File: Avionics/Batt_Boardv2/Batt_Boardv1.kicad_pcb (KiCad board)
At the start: 2 copper layers, 90.2 x 95.9 mm, 30 parts, among them J1 Conn_02x26_Odd_Even, J2 Conn_02x26_Odd_Even, Q1 IRF7458, Q2 IRF7458, U3 TMP36xS

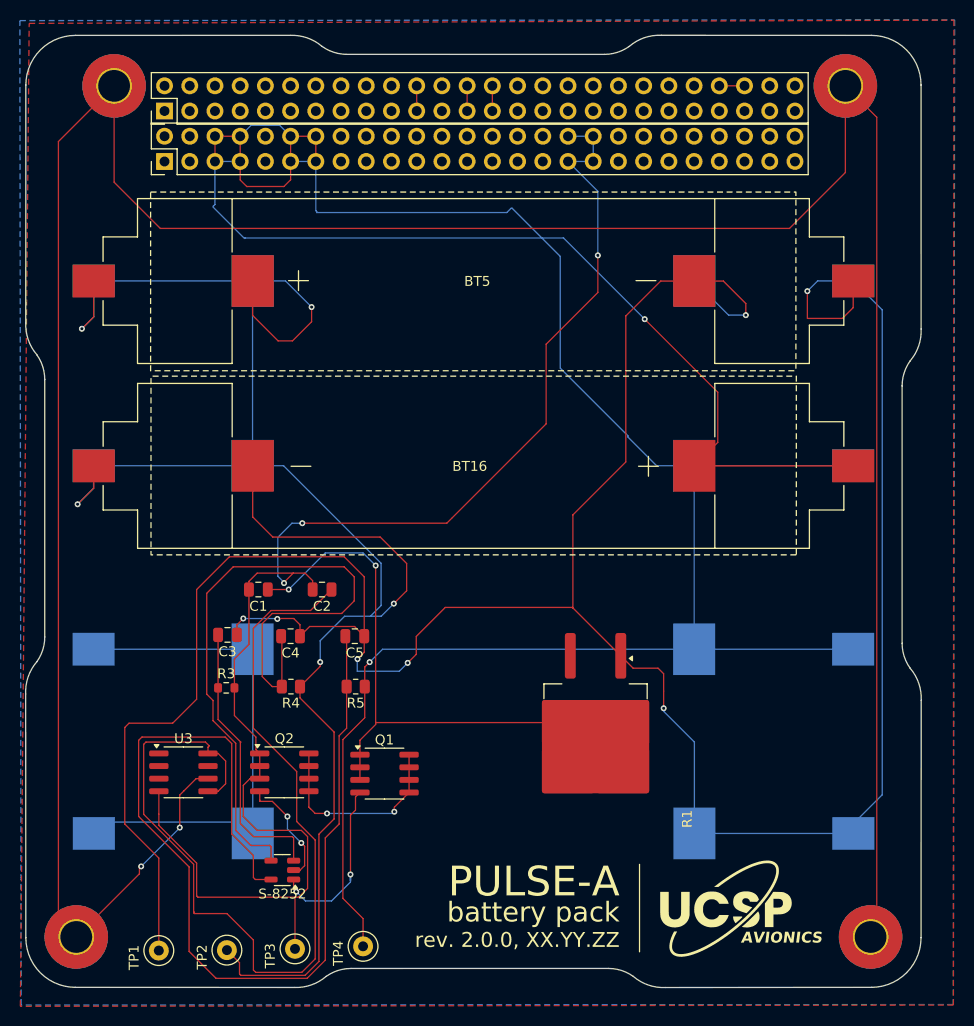
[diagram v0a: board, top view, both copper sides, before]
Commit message: zones added, but incorrectly
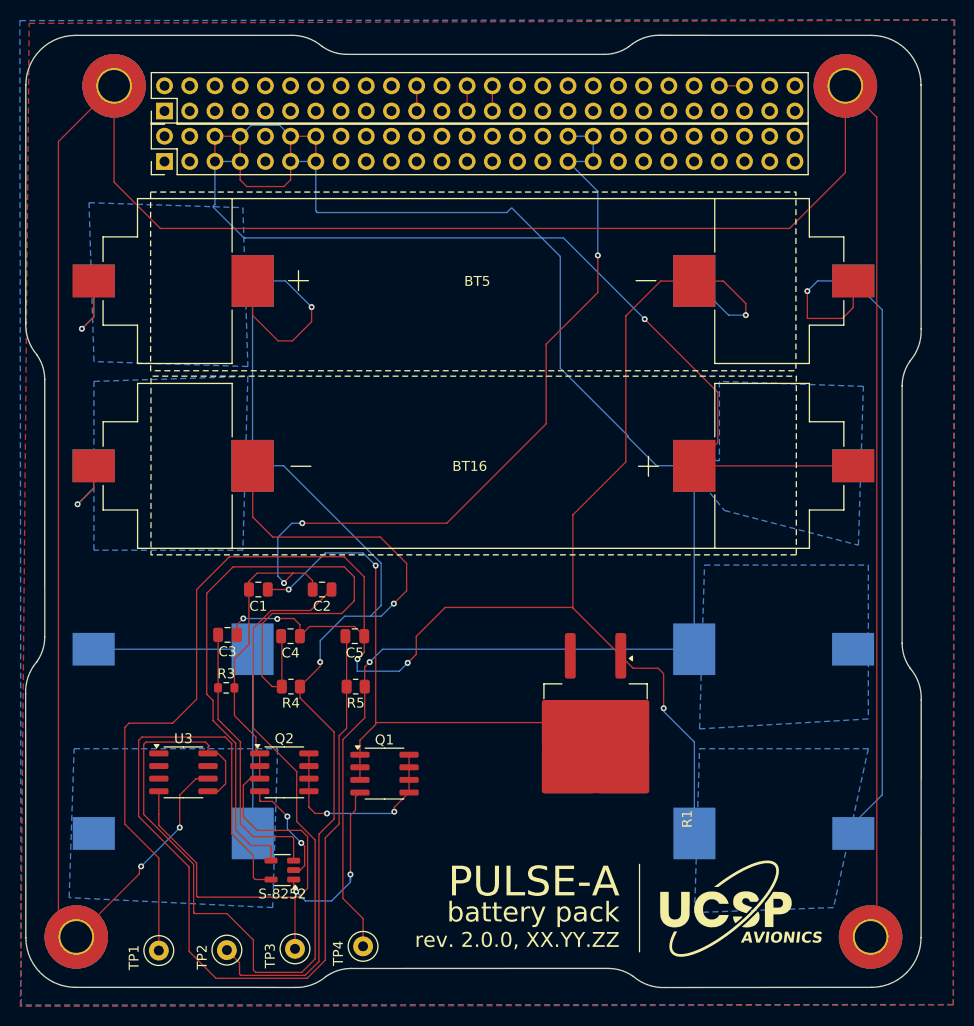
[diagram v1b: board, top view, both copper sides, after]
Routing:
- net /BATT_PRE_INH: track 298.4 -> 266.4 mm
- net /BM: track 195.8 -> 163.8 mm
- net /B-: track 287.0 -> 271.0 mm
- net Net-(BT1-BATT-): track 51.5 -> 37.8 mm
- added copper zone on B.Cu, net V_BATT
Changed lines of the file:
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@@
-	)
-	(segment
-		(start 166.953992 92.99071)
-		(end 182.963992 92.99071)
-		(width 0.1)
-		(layer "B.Cu")
-		(net 6)
 	)
 	(segment
@@
 	)
 	(segment
-		(start 166.95745 111.479203)
-		(end 182.96745 111.479203)
-		(width 0.1)
-		(layer "B.Cu")
-		(net 6)
-	)
-	(segment
 		(start 131.950334 115.242534)
 		(end 131.950334 119.438534)
@@
 	)
 	(segment
-		(start 166.979121 130.031863)
-		(end 182.989121 130.031863)
-		(width 0.1)
-		(layer "B.Cu")
-		(net 8)
-	)
-	(segment
 		(start 121.546667 108.384534)
 		(end 121.541334 108.379201)
@@
 	)
 	(segment
-		(start 122.471146 92.99071)
-		(end 106.461146 92.99071)
-		(width 0.1)
-		(layer "B.Cu")
-		(net 13)
-	)
-	(segment
 		(start 136.7028 106.8832)
 		(end 135.4328 108.1532)
@@
 	)
 	(segment
-		(start 122.49016 74.376)
-		(end 106.48016 74.376)
-		(width 0.1)
-		(layer "B.Cu")
-		(net 13)
-	)
-	(segment
 		(start 106.48016 78.00004)
 		(end 105.283 79.1972)
@@
 		(start 122.474604 111.479203)
 		(end 106.464604 111.479203)
-		(width 0.1)
-		(layer "B.Cu")
-		(net 14)
-	)
-	(segment
-		(start 107.627004 128.891134)
-		(end 121.355546 128.891134)
 		(width 0.1)
 		(layer "B.Cu")
@@
 			)
 		)
+	)
+	(zone
+		(net 77)
+		(net_name "V_BATT")
+		(layer "B.Cu")
+		(hatch edge 0.5)
+		(priority 5)
+		(connect_pads
+			(clearance 0.254)
+		)
+		(min_thickness 0.25)
+		(filled_areas_thickness no)
+		(fill yes
+			(thermal_gap 0.5)
+			(thermal_bridge_width 0.5)
+		)
+		(polygon
+			(pts
+				(xy 169.5 84.5) (xy 169.5 92.5) (xy 165.5 92) (xy 170 97.5) (xy 183.5 101) (xy 184 85)
+			)
+		)
+	)
+	(zone
+		(net 77)
+		(net_name "V_BATT")
+		(layer "B.Cu")
+		(hatch edge 0.5)
+		(priority 6)
+		(connect_pads
+			(clearance 0.254)
+		)
+		(min_thickness 7)
+		(filled_areas_thickness no)
+		(fill yes
+			(thermal_gap 0.5)
+			(thermal_bridge_width 7)
+		)
+		(polygon
+			(pts
+				(xy 106.5 84.5) (xy 122 84) (xy 121.5 101.5) (xy 106.5 101.5)
+			)
+		)
+	)
+	(zone
+		(net 77)
+		(net_name "V_BATT")
+		(layer "B.Cu")
+		(hatch edge 0.5)
+		(priority 2)
+		(connect_pads
+			(clearance 0.254)
+		)
+		(min_thickness 7)
+		(filled_areas_thickness no)
+		(fill yes
+			(thermal_gap 0.5)
+			(thermal_bridge_width 7)
+		)
+		(polygon
+			(pts
+				(xy 104.5 121.5) (xy 125 121.5) (xy 124.5 137.5) (xy 104 136.5)
+			)
+		)
+	)
+	(zone
+		(net 77)
+		(net_name "V_BATT")
+		(layer "B.Cu")
+		(hatch edge 0.5)
+		(priority 4)
+		(connect_pads
+			(clearance 0.254)
+		)
+		(min_thickness 7)
+		(filled_areas_thickness no)
+		(fill yes
+			(thermal_gap 0.5)
+			(thermal_bridge_width 7)
+		)
+		(polygon
+			(pts
+				(xy 168 103) (xy 184.5 103) (xy 184.5 118.5) (xy 167.5 119.5)
+			)
+		)
+	)
+	(zone
+		(net 77)
+		(net_name "V_BATT")
+		(layer "B.Cu")
+		(hatch edge 0.5)
+		(priority 3)
+		(connect_pads
+			(clearance 0.254)
+		)
+		(min_thickness 7)
+		(filled_areas_thickness no)
+		(fill yes
+			(thermal_gap 0.5)
+			(thermal_bridge_width 7)
+		)
+		(polygon
+			(pts
+				(xy 167.5 121.5) (xy 184.5 121.5) (xy 181 137.5) (xy 167 138)
+			)
+		)
+	)
+	(zone
+		(net 77)
+		(net_name "V_BATT")
+		(layer "B.Cu")
+		(hatch edge 0.5)
+		(priority 7)
+		(connect_pads
+			(clearance 0.254)
+		)
+		(min_thickness 7)
+		(filled_areas_thickness no)
+		(fill yes
+			(thermal_gap 0.5)
+			(thermal_bridge_width 7)
+		)
+		(polygon
+			(pts
+				(xy 106 66.5) (xy 121.5 67) (xy 122 83) (xy 106.5 82.5)
+			)
+		)

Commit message: 12/17/2024, Sephora Poteau: Made power traces 0.7mm and fixed zones on front and back plate
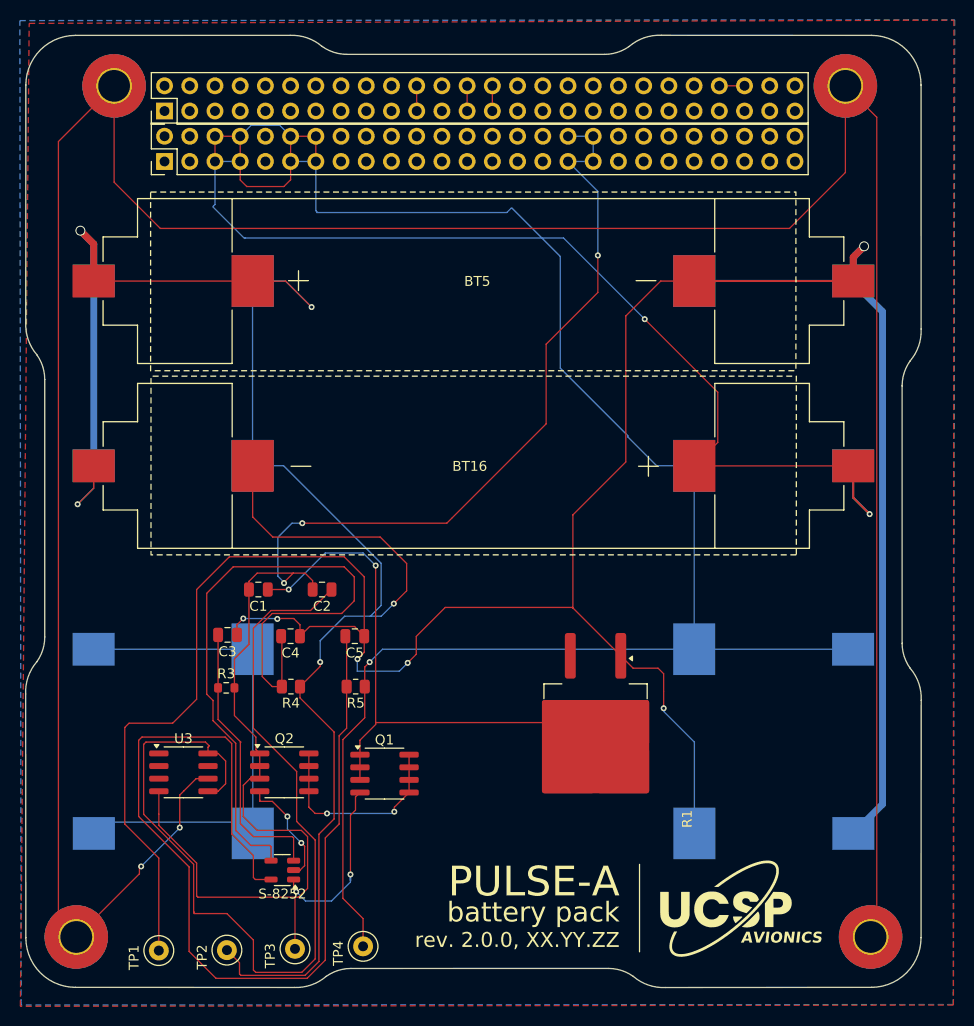
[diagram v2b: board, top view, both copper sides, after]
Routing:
- net /BM: track 163.8 -> 193.4 mm
- net /BATT_PRE_INH: track 266.4 -> 293.5 mm, vias 2 -> 3
- net Net-(BT1-BATT-): track 37.8 -> 51.5 mm
- net /B-: track 271.0 -> 282.4 mm, vias 7 -> 6
- removed copper zone on B.Cu, net V_BATT
